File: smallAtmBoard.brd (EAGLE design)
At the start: 66.1 x 51.7 mm, 29 parts, among them IC1 ATMEGA-328P, IC2 7805-V, Y1 16MHz

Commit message: smaller header
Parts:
- SV2: device bauteile_jbt:FE08 -> bauteile_jbt:FE08-1-RAW
- SV3: device con-lsta:FE06 -> bauteile_jbt:FE06-1-RAW
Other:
- board text added: "D0"
- board text added: "D1"
- board text added: "Serial"
- board text removed: "D12"
- board text removed: "D5"
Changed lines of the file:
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@@
 <setting verticaltext="up"/>
 </settings>
-<grid distance="5" unitdist="mil" unit="mil" style="lines" multiple="1" display="yes" altdistance="100" altunitdist="mil" altunit="mil"/>
+<grid distance="2" unitdist="mil" unit="mil" style="lines" multiple="1" display="yes" altdistance="100" altunitdist="mil" altunit="mil"/>
 <layers>
-<layer number="1" name="Top" color="4" fill="1" visible="no" active="yes"/>
+<layer number="1" name="Top" color="4" fill="1" visible="yes" active="yes"/>
 <layer number="2" name="Route2" color="1" fill="3" visible="no" active="no"/>
 <layer number="3" name="Route3" color="4" fill="3" visible="no" active="no"/>
@@
 <layer number="17" name="Pads" color="2" fill="1" visible="yes" active="yes"/>
 <layer number="18" name="Vias" color="14" fill="1" visible="yes" active="yes"/>
-<layer number="19" name="Unrouted" color="6" fill="1" visible="no" active="yes"/>
-<layer number="20" name="Dimension" color="15" fill="1" visible="no" active="yes"/>
-<layer number="21" name="tPlace" color="7" fill="1" visible="no" active="yes"/>
+<layer number="19" name="Unrouted" color="6" fill="1" visible="yes" active="yes"/>
+<layer number="20" name="Dimension" color="15" fill="1" visible="yes" active="yes"/>
+<layer number="21" name="tPlace" color="7" fill="1" visible="yes" active="yes"/>
 <layer number="22" name="bPlace" color="7" fill="1" visible="no" active="yes"/>
-<layer number="23" name="tOrigins" color="15" fill="1" visible="no" active="yes"/>
+<layer number="23" name="tOrigins" color="15" fill="1" visible="yes" active="yes"/>
 <layer number="24" name="bOrigins" color="15" fill="1" visible="no" active="yes"/>
 <layer number="25" name="tNames" color="7" fill="1" visible="no" active="yes"/>
 <layer number="26" name="bNames" color="7" fill="1" visible="no" active="yes"/>
 <layer number="27" name="tValues" color="7" fill="1" visible="no" active="yes"/>
-<layer number="28" name="bValues" color="7" fill="1" visible="no" active="yes"/>
-<layer number="29" name="tStop" color="7" fill="3" visible="no" active="yes"/>
+<layer number="28" name="bValues" color="7" fill="1" visible="yes" active="yes"/>
+<layer number="29" name="tStop" color="7" fill="3" visible="yes" active="yes"/>
 <layer number="30" name="bStop" color="7" fill="6" visible="no" active="yes"/>
 <layer number="31" name="tCream" color="7" fill="4" visible="no" active="yes"/>
@@
 <layer number="42" name="bRestrict" color="1" fill="10" visible="no" active="yes"/>
 <layer number="43" name="vRestrict" color="2" fill="10" visible="no" active="yes"/>
-<layer number="44" name="Drills" color="7" fill="1" visible="yes" active="yes"/>
+<layer number="44" name="Drills" color="7" fill="1" visible="no" active="yes"/>
 <layer number="45" name="Holes" color="7" fill="1" visible="no" active="yes"/>
 <layer number="46" name="Milling" color="3" fill="1" visible="no" active="yes"/>
@@
 <text x="40.386" y="25.908" size="1.27" layer="28" font="vector" ratio="10" rot="MR90">D2</text>
 <text x="40.386" y="43.307" size="1.27" layer="28" font="vector" ratio="10" rot="MR90">D9</text>
-<text x="40.386" y="35.56" size="1.27" layer="28" font="vector" ratio="10" rot="MR90">D12</text>
-<text x="40.386" y="32.385" size="1.27" layer="28" font="vector" ratio="10" rot="MR90">D5</text>
+<text x="40.4876" y="35.6616" size="1.27" layer="28" font="vector" ratio="10" rot="MR90">12</text>
+<text x="40.4876" y="33.7566" size="1.27" layer="28" font="vector" ratio="10" rot="MR90">5</text>
 <text x="7.4295" y="35.687" size="1.27" layer="28" font="vector" ratio="10" rot="SMR270">GND</text>
 <text x="43.1165" y="2.6289" size="1.27" layer="28" font="vector" ratio="10" rot="MR180">SCL</text>
@@
 <text x="26.3779" y="1.1303" size="1.27" layer="27" font="vector" ratio="10" rot="R90">LCD/KBD</text>
 <text x="45.0977" y="1.7399" size="1.27" layer="27" font="vector" ratio="10" rot="R180">I2C</text>
+<text x="57.9628" y="21.6408" size="1.27" layer="27" font="vector" ratio="10" rot="R90">Serial</text>
+<text x="52.8193" y="13.3731" size="1.27" layer="28" font="vector" ratio="10" rot="MR0">D0</text>
+<text x="52.8701" y="15.6591" size="1.27" layer="28" font="vector" ratio="10" rot="MR0">D1</text>
+<text x="52.7685" y="38.7731" size="1.27" layer="28" font="vector" ratio="10" rot="MR0">D6</text>
+<text x="52.7685" y="41.3131" size="1.27" layer="28" font="vector" ratio="10" rot="MR0">D7</text>
+<text x="52.8193" y="43.7007" size="1.27" layer="28" font="vector" ratio="10" rot="MR0">D8</text>
 </plain>
 <attributes>
@@
 <element name="R22" library="bauteile_jbt" package="R_0207/2V" value="2.2k" x="58.801" y="12.319" rot="R90"/>
 <element name="R23" library="bauteile_jbt" package="R_0207/2V" value="2.2k" x="62.23" y="12.319" rot="R90"/>
-<element name="SV3" library="con-lsta" package="FE06" value="" x="43.2562" y="17.8054" rot="R270">
-<attribute name="OC_FARNELL" value="unknown" x="43.2562" y="17.8054" size="1.778" layer="27" rot="R270" display="off"/>
-<attribute name="OC_NEWARK" value="unknown" x="43.2562" y="17.8054" size="1.778" layer="27" rot="R270" display="off"/>
-<attribute name="MF" value="" x="43.2562" y="17.8054" size="1.778" layer="27" rot="R270" display="off"/>
-<attribute name="MPN" value="" x="43.2562" y="17.8054" size="1.778" layer="27" rot="R270" display="off"/>
-</element>
+<element name="SV3" library="bauteile_jbt" package="FE06-1-RAW" value="" x="43.2562" y="17.8054" rot="R270"/>
 <element name="CON6" library="bauteile_jbt" package="FE03-2" value="" x="31.75" y="5.08" smashed="yes">
 <attribute name="NAME" x="31.75" y="8.509" size="1.27" layer="25" font="vector" ratio="10"/>
@@
 <element name="PAD5" library="bauteile_jbt" package="PAD1,6/0,8" value="D1" x="11.43" y="8.89"/>
 <element name="PAD6" library="bauteile_jbt" package="PAD1,6/0,8" value="D1" x="11.43" y="6.35"/>
-<element name="SV2" library="bauteile_jbt" package="FE08" value="" x="43.307" y="35.56" rot="R90">
-<attribute name="MF" value="" x="43.307" y="35.56" size="1.778" layer="27" rot="R90" display="off"/>
-<attribute name="OC_FARNELL" value="unknown" x="43.307" y="35.56" size="1.778" layer="27" rot="R90" display="off"/>
-<attribute name="OC_NEWARK" value="unknown" x="43.307" y="35.56" size="1.778" layer="27" rot="R90" display="off"/>
-<attribute name="MPN" value="" x="43.307" y="35.56" size="1.778" layer="27" rot="R90" display="off"/>
-</element>
+<element name="SV2" library="bauteile_jbt" package="FE08-1-RAW" value="" x="43.307" y="35.56" rot="R90"/>
 <element name="U$6" library="bauteile_jbt" package="SOLDER" value="" x="11.7094" y="3.6322" rot="R180"/>
 <element name="U$7" library="bauteile_jbt" package="COMP" value="" x="11.6332" y="3.6322"/>

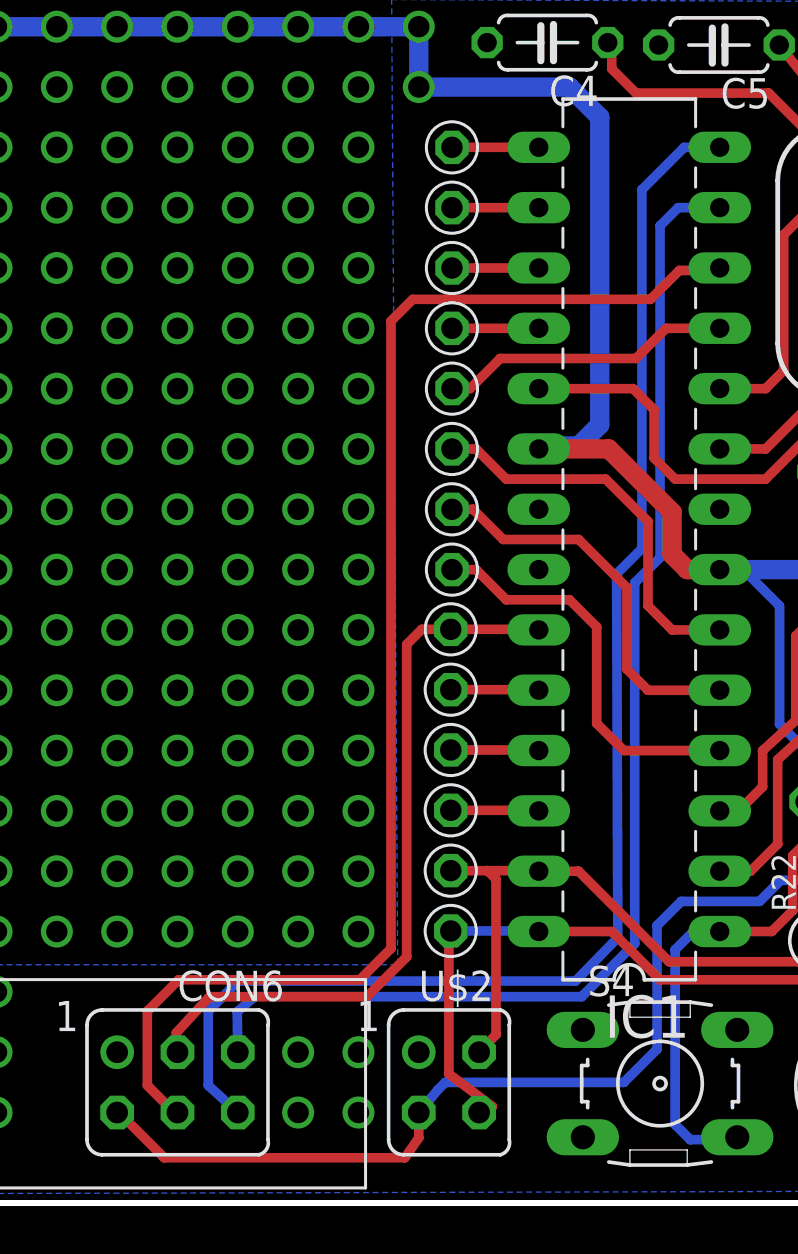
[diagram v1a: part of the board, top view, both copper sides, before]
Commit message: standartize pins on LCD connector
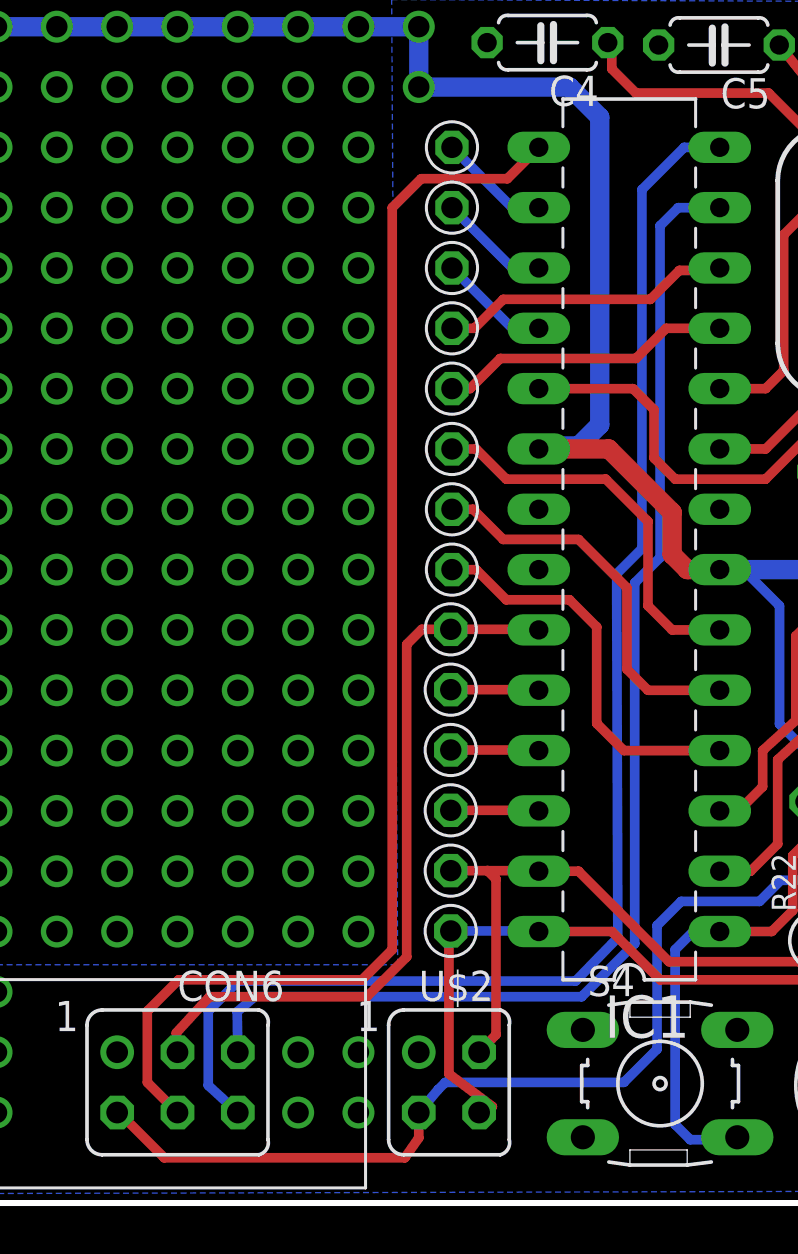
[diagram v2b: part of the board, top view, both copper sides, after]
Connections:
- net AT-PD10: now also SV2.8; no longer SV2.7
- net AT-PD11: now also SV2.7; no longer SV2.6
- net AT-PD12: now also SV2.6; no longer SV2.5
- net AT-PD6: now also SV2.5; no longer CON6.4
- net AT-PD9: now also CON6.4; no longer SV2.8
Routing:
- net AT-PD9: track 3.66 -> 54.6 mm
- net AT-PD6: track 57.4 -> 12.3 mm
- net AT-PD10: track 3.66 -> 4.71 mm
- net AT-PD12: track 3.66 -> 4.71 mm
- net AT-PD11: track 3.66 -> 4.71 mm
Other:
- board text added: "1"
- board text added: "2"
- board text added: "6"
- board text added: "D10"
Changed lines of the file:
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@@
 <layer number="14" name="Route14" color="1" fill="6" visible="no" active="no"/>
 <layer number="15" name="Route15" color="4" fill="6" visible="no" active="no"/>
-<layer number="16" name="Bottom" color="1" fill="1" visible="no" active="yes"/>
+<layer number="16" name="Bottom" color="1" fill="1" visible="yes" active="yes"/>
 <layer number="17" name="Pads" color="2" fill="1" visible="yes" active="yes"/>
 <layer number="18" name="Vias" color="14" fill="1" visible="yes" active="yes"/>
@@
 <layer number="25" name="tNames" color="7" fill="1" visible="no" active="yes"/>
 <layer number="26" name="bNames" color="7" fill="1" visible="no" active="yes"/>
-<layer number="27" name="tValues" color="7" fill="1" visible="no" active="yes"/>
+<layer number="27" name="tValues" color="7" fill="1" visible="yes" active="yes"/>
 <layer number="28" name="bValues" color="7" fill="1" visible="yes" active="yes"/>
 <layer number="29" name="tStop" color="7" fill="3" visible="yes" active="yes"/>
@@
 <text x="40.386" y="23.114" size="1.27" layer="28" font="vector" ratio="10" rot="MR90">A0</text>
 <text x="40.386" y="25.908" size="1.27" layer="28" font="vector" ratio="10" rot="MR90">D2</text>
-<text x="40.386" y="43.307" size="1.27" layer="28" font="vector" ratio="10" rot="MR90">D9</text>
-<text x="40.4876" y="35.6616" size="1.27" layer="28" font="vector" ratio="10" rot="MR90">12</text>
+<text x="40.386" y="43.307" size="1.27" layer="28" font="vector" ratio="10" rot="MR90">D10</text>
+<text x="40.5892" y="38.2524" size="1.27" layer="28" font="vector" ratio="10" rot="MR90">12</text>
 <text x="40.4876" y="33.7566" size="1.27" layer="28" font="vector" ratio="10" rot="MR90">5</text>
 <text x="7.4295" y="35.687" size="1.27" layer="28" font="vector" ratio="10" rot="SMR270">GND</text>
@@
 <text x="65.2145" y="22.2885" size="1.27" layer="28" font="vector" ratio="10" rot="MR270">R</text>
 <text x="24.1808" y="0.9906" size="1.016" layer="28" font="vector" rot="MR0">github.com/benoitjoh 2018</text>
-<text x="41.7576" y="43.6626" size="1.27" layer="27" font="vector" ratio="10" rot="R90">D9</text>
-<text x="41.6052" y="35.6616" size="1.27" layer="27" font="vector" ratio="10" rot="R90">12</text>
-<text x="41.656" y="33.6804" size="1.27" layer="27" font="vector" ratio="10" rot="R90">5</text>
-<text x="41.656" y="25.7302" size="1.27" layer="27" font="vector" ratio="10" rot="R90">D2</text>
-<text x="41.6052" y="22.86" size="1.27" layer="27" font="vector" ratio="10" rot="R90">A0</text>
-<text x="41.656" y="10.3632" size="1.27" layer="27" font="vector" ratio="10" rot="R90">A5</text>
-<text x="41.656" y="28.8036" size="1.27" layer="27" font="vector" ratio="10" rot="R90">3</text>
-<text x="41.6814" y="31.0134" size="1.27" layer="27" font="vector" ratio="10" rot="R90">4</text>
-<text x="31.0515" y="0.5715" size="1.27" layer="28" font="vector" ratio="10" rot="MR90">D6</text>
+<text x="41.91" y="42.7482" size="1.27" layer="27" font="vector" ratio="10" rot="R90">D10</text>
+<text x="41.91" y="36.2204" size="1.27" layer="27" font="vector" ratio="10" rot="R90">6</text>
+<text x="41.91" y="33.7312" size="1.27" layer="27" font="vector" ratio="10" rot="R90">5</text>
+<text x="41.91" y="25.7302" size="1.27" layer="27" font="vector" ratio="10" rot="R90">D2</text>
+<text x="41.91" y="22.86" size="1.27" layer="27" font="vector" ratio="10" rot="R90">A0</text>
+<text x="41.91" y="10.4648" size="1.27" layer="27" font="vector" ratio="10" rot="R90">A5</text>
+<text x="41.8592" y="28.7528" size="1.27" layer="27" font="vector" ratio="10" rot="R90">3</text>
+<text x="41.8846" y="31.3182" size="1.27" layer="27" font="vector" ratio="10" rot="R90">4</text>
+<text x="31.0515" y="0.5715" size="1.27" layer="28" font="vector" ratio="10" rot="MR90">D9</text>
 <text x="26.3779" y="1.1303" size="1.27" layer="27" font="vector" ratio="10" rot="R90">LCD/KBD</text>
 <text x="45.0977" y="1.7399" size="1.27" layer="27" font="vector" ratio="10" rot="R180">I2C</text>
@@
 <text x="52.7685" y="41.3131" size="1.27" layer="28" font="vector" ratio="10" rot="MR0">D7</text>
 <text x="52.8193" y="43.7007" size="1.27" layer="28" font="vector" ratio="10" rot="MR0">D8</text>
+<text x="40.4876" y="36.2458" size="1.27" layer="28" font="vector" ratio="10" rot="MR90">6</text>
+<text x="40.4876" y="31.3182" size="1.27" layer="28" font="vector" ratio="10" rot="MR90">4</text>
+<text x="40.4876" y="28.9814" size="1.27" layer="28" font="vector" ratio="10" rot="MR90">3</text>
+<text x="41.9608" y="38.2524" size="1.27" layer="27" font="vector" ratio="10" rot="R90">12</text>
+<text x="41.8592" y="18.5928" size="1.27" layer="27" font="vector" ratio="10" rot="R90">2</text>
+<text x="41.8592" y="21.1836" size="1.27" layer="27" font="vector" ratio="10" rot="R90">1</text>
+<text x="41.8592" y="16.1544" size="1.27" layer="27" font="vector" ratio="10" rot="R90">3</text>
+<text x="41.8592" y="13.6144" size="1.27" layer="27" font="vector" ratio="10" rot="R90">4</text>
 </plain>
 <attributes>
@@
 <signal name="AT-PD6">
 <contactref element="IC1" pad="12"/>
-<contactref element="CON6" pad="4"/>
-<wire x1="31.8008" y1="9.398" x2="39.4208" y2="9.398" width="0.4064" layer="1"/>
-<wire x1="39.4208" y1="9.398" x2="40.7416" y2="10.7188" width="0.4064" layer="1"/>
-<wire x1="40.7416" y1="10.7188" x2="40.7416" y2="37.1348" width="0.4064" layer="1"/>
-<wire x1="40.7416" y1="37.1348" x2="41.656" y2="38.0492" width="0.4064" layer="1"/>
-<wire x1="41.656" y1="38.0492" x2="51.6636" y2="38.0492" width="0.4064" layer="1"/>
 <wire x1="51.6636" y1="38.0492" x2="52.8828" y2="39.2684" width="0.4064" layer="1"/>
 <wire x1="52.8828" y1="39.2684" x2="54.479509375" y2="39.2684" width="0.4064" layer="1"/>
 <wire x1="54.479509375" y1="39.2684" x2="54.5825625" y2="39.371453125" width="0.4064" layer="1"/>
-<wire x1="31.8008" y1="9.398" x2="30.48" y2="8.0772" width="0.4064" layer="1"/>
-<wire x1="30.48" y1="8.0772" x2="30.48" y2="4.953" width="0.4064" layer="1"/>
-<wire x1="30.48" y1="4.953" x2="31.623" y2="3.81" width="0.4064" layer="1"/>
-<wire x1="31.623" y1="3.81" x2="31.75" y2="3.81" width="0.4064" layer="1"/>
+<contactref element="SV2" pad="5"/>
+<wire x1="51.6636" y1="38.0492" x2="45.466" y2="38.0492" width="0.4064" layer="1"/>
+<wire x1="45.466" y1="38.0492" x2="44.2468" y2="36.83" width="0.4064" layer="1"/>
+<wire x1="44.2468" y1="36.83" x2="43.307" y2="36.83" width="0.4064" layer="1"/>
 </signal>
 <signal name="AT-PD13">
@@
 <signal name="AT-PD10">
 <contactref element="IC1" pad="16"/>
-<contactref element="SV2" pad="7"/>
-<wire x1="43.307" y1="41.91" x2="46.9625625" y2="41.91" width="0.4064" layer="1"/>
-<wire x1="46.9625625" y1="41.91" x2="46.9625625" y2="41.911453125" width="0.4064" layer="1"/>
+<contactref element="SV2" pad="8"/>
+<wire x1="43.307" y1="44.45" x2="45.845546875" y2="41.911453125" width="0.4064" layer="16"/>
+<wire x1="45.845546875" y1="41.911453125" x2="46.9625625" y2="41.911453125" width="0.4064" layer="16"/>
 </signal>
 <signal name="AT-PD9">
 <contactref element="IC1" pad="15"/>
-<contactref element="SV2" pad="8"/>
-<wire x1="43.307" y1="44.45" x2="46.9625625" y2="44.45" width="0.4064" layer="1"/>
-<wire x1="46.9625625" y1="44.45" x2="46.9625625" y2="44.451453125" width="0.4064" layer="1"/>
+<contactref element="CON6" pad="4"/>
+<wire x1="31.75" y1="3.81" x2="30.48" y2="5.08" width="0.4064" layer="1"/>
+<wire x1="30.48" y1="5.08" x2="30.48" y2="8.0772" width="0.4064" layer="1"/>
+<wire x1="30.48" y1="8.0772" x2="31.8008" y2="9.398" width="0.4064" layer="1"/>
+<wire x1="31.8008" y1="9.398" x2="39.5224" y2="9.398" width="0.4064" layer="1"/>
+<wire x1="39.5224" y1="9.398" x2="40.7924" y2="10.668" width="0.4064" layer="1"/>
+<wire x1="40.7924" y1="10.668" x2="40.7924" y2="41.91" width="0.4064" layer="1"/>
+<wire x1="40.7924" y1="41.91" x2="42.0116" y2="43.1292" width="0.4064" layer="1"/>
+<wire x1="42.0116" y1="43.1292" x2="45.640309375" y2="43.1292" width="0.4064" layer="1"/>
+<wire x1="45.640309375" y1="43.1292" x2="46.9625625" y2="44.451453125" width="0.4064" layer="1"/>
 </signal>
 <signal name="AT-PD8">
@@
 <signal name="AT-PD12">
 <contactref element="IC1" pad="18"/>
-<contactref element="SV2" pad="5"/>
-<wire x1="43.307" y1="36.83" x2="46.9625625" y2="36.83" width="0.4064" layer="1"/>
-<wire x1="46.9625625" y1="36.83" x2="46.9625625" y2="36.831453125" width="0.4064" layer="1"/>
+<contactref element="SV2" pad="6"/>
+<wire x1="43.307" y1="39.37" x2="45.845546875" y2="36.831453125" width="0.4064" layer="16"/>
+<wire x1="45.845546875" y1="36.831453125" x2="46.9625625" y2="36.831453125" width="0.4064" layer="16"/>
 </signal>
 <signal name="AT-PD11">
 <contactref element="IC1" pad="17"/>
-<contactref element="SV2" pad="6"/>
-<wire x1="43.307" y1="39.37" x2="46.9625625" y2="39.37" width="0.4064" layer="1"/>
-<wire x1="46.9625625" y1="39.37" x2="46.9625625" y2="39.371453125" width="0.4064" layer="1"/>
+<contactref element="SV2" pad="7"/>
+<wire x1="43.307" y1="41.91" x2="45.845546875" y2="39.371453125" width="0.4064" layer="16"/>
+<wire x1="45.845546875" y1="39.371453125" x2="46.9625625" y2="39.371453125" width="0.4064" layer="16"/>
 </signal>
 <signal name="N$1">
